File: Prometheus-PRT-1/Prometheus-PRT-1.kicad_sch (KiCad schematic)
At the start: 16 parts, among them J1 Conn_02x10_Odd_Even, J2 AppleIIBus, U1 74LS74, U2 74LS74, U3 74LS00, U4 74LS374, U5 74LS30, U6 74LS08, U7 27C64, U8 74LS08, U9 74LS00

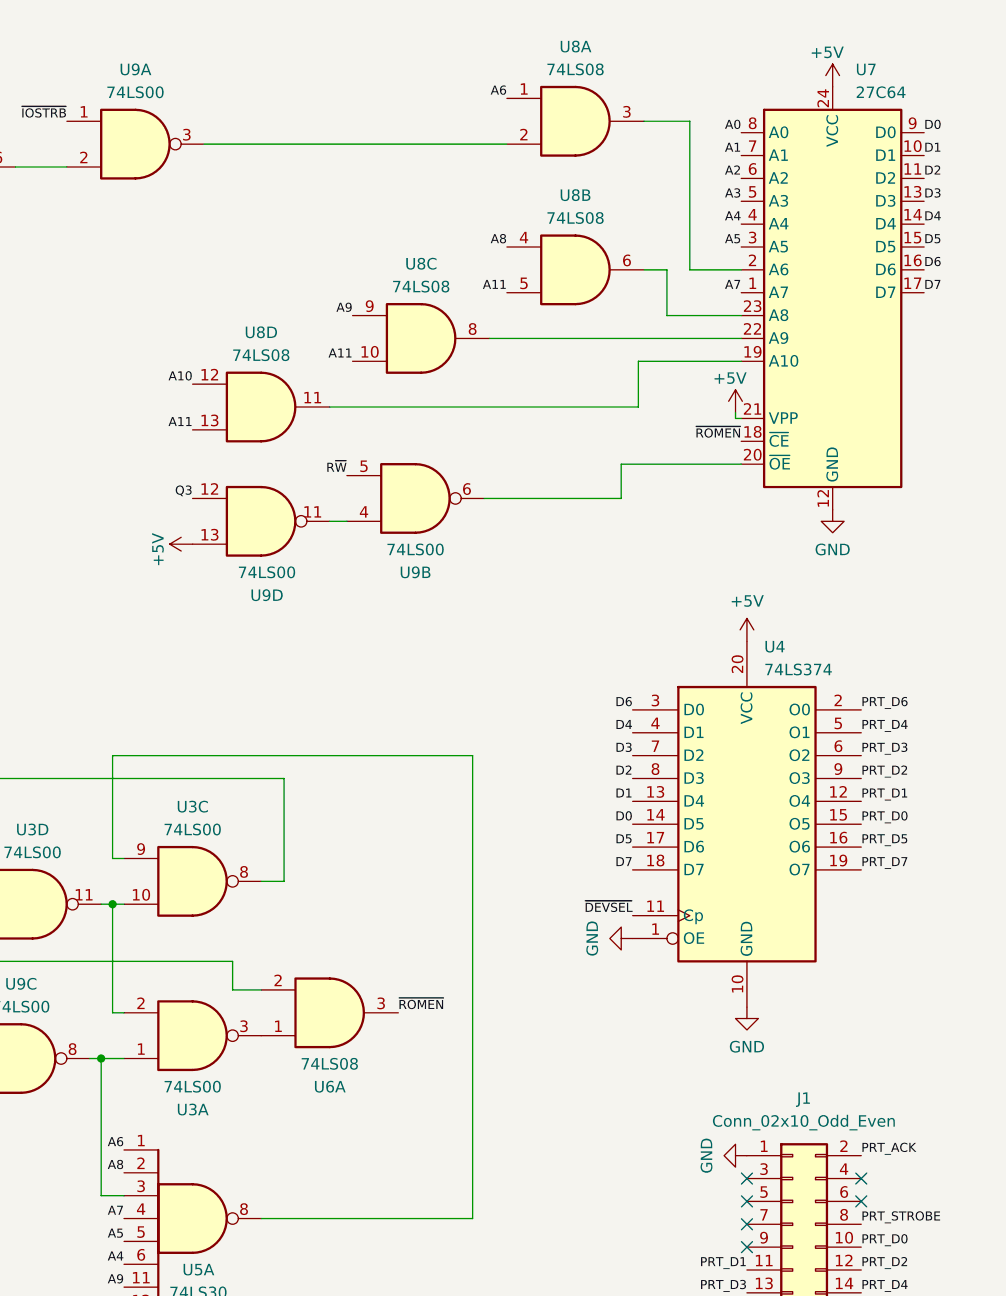
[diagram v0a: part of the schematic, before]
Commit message: Fix mis-id'd EPROM part in the PRT-1 schematic
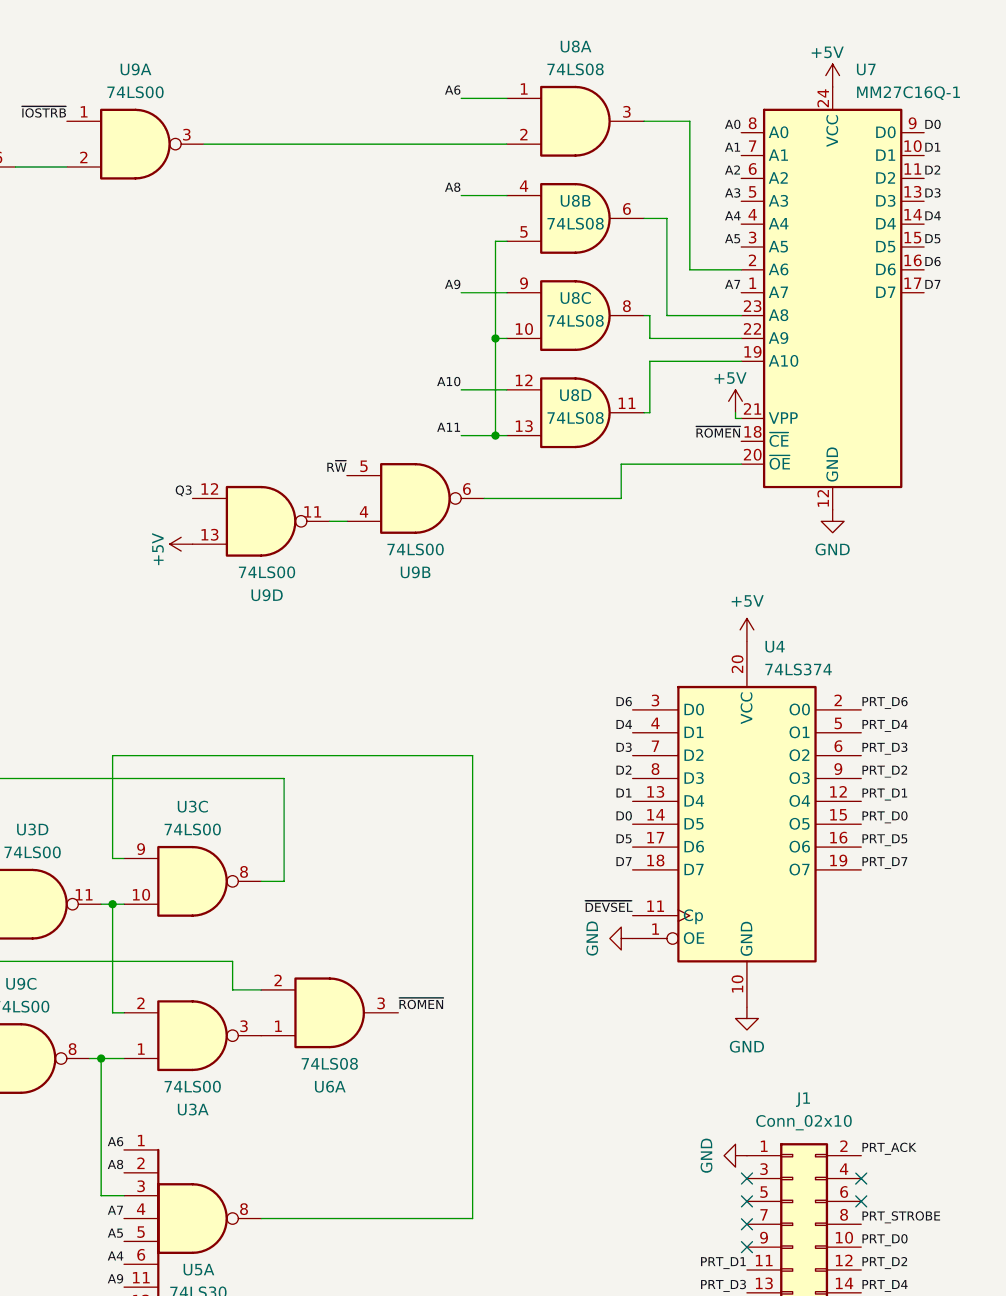
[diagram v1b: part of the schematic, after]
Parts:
- J1: value Conn_02x10_Odd_Even -> Conn_02x10
- U7: value 27C64 -> MM27C16Q-1
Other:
- moved on the sheet: U8B, U8C, U8D
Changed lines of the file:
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@@
   (junction (at 99.695 41.275) (diameter 0) (color 0 0 0 0)
   )
+  (junction (at 205.105 52.705) (diameter 0) (color 0 0 0 0)
+  )
   (junction (at 63.5 168.91) (diameter 0) (color 0 0 0 0)
   )
@@
   )
   (junction (at 49.53 168.91) (diameter 0) (color 0 0 0 0)
+  )
+  (junction (at 205.105 63.5) (diameter 0) (color 0 0 0 0)
   )
   (junction (at 109.22 102.235) (diameter 0) (color 0 0 0 0)
@@
     (stroke (width 0) (type default))
   )
-  (wire (pts (xy 220.98 55.245) (xy 232.41 55.245))
+  (wire (pts (xy 222.25 55.245) (xy 232.41 55.245))
     (stroke (width 0) (type default))
   )
@@
     (stroke (width 0) (type default))
   )
+  (wire (pts (xy 222.25 52.705) (xy 232.41 52.705))
+    (stroke (width 0) (type default))
+  )
   (wire (pts (xy 49.53 168.91) (xy 49.53 171.45))
     (stroke (width 0) (type default))
@@
     (stroke (width 0) (type default))
   )
+  (wire (pts (xy 201.295 63.5) (xy 205.105 63.5))
+    (stroke (width 0) (type default))
+  )
   (wire (pts (xy 97.155 41.91) (xy 97.155 41.275))
     (stroke (width 0) (type default))
   )
-  (wire (pts (xy 186.69 60.325) (xy 220.98 60.325))
-    (stroke (width 0) (type default))
-  )
   (wire (pts (xy 72.39 29.845) (xy 72.39 47.625))
     (stroke (width 0) (type default))
   )
+  (wire (pts (xy 205.105 52.705) (xy 205.105 63.5))
+    (stroke (width 0) (type default))
+  )
   (wire (pts (xy 114.3 86.36) (xy 114.3 104.775))
     (stroke (width 0) (type default))
@@
     (stroke (width 0) (type default))
   )
+  (wire (pts (xy 201.295 26.035) (xy 206.375 26.035))
+    (stroke (width 0) (type default))
+  )
   (wire (pts (xy 77.47 168.91) (xy 84.455 168.91))
     (stroke (width 0) (type default))
@@
     (stroke (width 0) (type default))
   )
-  (wire (pts (xy 224.155 50.165) (xy 224.155 45.085))
+  (wire (pts (xy 224.155 50.165) (xy 224.155 39.37))
     (stroke (width 0) (type default))
   )
@@
     (stroke (width 0) (type default))
   )
+  (wire (pts (xy 222.25 60.96) (xy 221.615 60.96))
+    (stroke (width 0) (type default))
+  )
+  (wire (pts (xy 206.375 52.705) (xy 205.105 52.705))
+    (stroke (width 0) (type default))
+  )
   (wire (pts (xy 63.5 191.77) (xy 63.5 194.31))
     (stroke (width 0) (type default))
@@
     (stroke (width 0) (type default))
   )
+  (wire (pts (xy 205.105 41.91) (xy 206.375 41.91))
+    (stroke (width 0) (type default))
+  )
   (wire (pts (xy 97.155 38.735) (xy 112.395 38.735))
     (stroke (width 0) (type default))
@@
     (stroke (width 0) (type default))
   )
-  (wire (pts (xy 224.155 45.085) (xy 221.615 45.085))
+  (wire (pts (xy 222.25 50.165) (xy 222.25 52.705))
+    (stroke (width 0) (type default))
+  )
+  (wire (pts (xy 224.155 39.37) (xy 221.615 39.37))
     (stroke (width 0) (type default))
   )
@@
     (stroke (width 0) (type default))
   )
+  (wire (pts (xy 201.295 36.83) (xy 206.375 36.83))
+    (stroke (width 0) (type default))
+  )
   (wire (pts (xy 105.41 168.91) (xy 119.38 168.91))
     (stroke (width 0) (type default))
@@
     (stroke (width 0) (type default))
   )
+  (wire (pts (xy 205.105 52.705) (xy 205.105 41.91))
+    (stroke (width 0) (type default))
+  )
   (wire (pts (xy 100.33 91.44) (xy 100.33 95.885))
     (stroke (width 0) (type default))
@@
     (stroke (width 0) (type default))
   )
+  (wire (pts (xy 205.105 63.5) (xy 206.375 63.5))
+    (stroke (width 0) (type default))
+  )
   (wire (pts (xy 63.5 168.91) (xy 49.53 168.91))
     (stroke (width 0) (type default))
@@
     (stroke (width 0) (type default))
   )
-  (wire (pts (xy 204.47 52.705) (xy 232.41 52.705))
+  (wire (pts (xy 221.615 50.165) (xy 222.25 50.165))
     (stroke (width 0) (type default))
   )
@@
     (stroke (width 0) (type default))
   )
-  (wire (pts (xy 220.98 60.325) (xy 220.98 55.245))
+  (wire (pts (xy 222.25 60.96) (xy 222.25 55.245))
+    (stroke (width 0) (type default))
+  )
+  (wire (pts (xy 201.295 58.42) (xy 206.375 58.42))
     (stroke (width 0) (type default))
   )
@@
   )
   (wire (pts (xy 94.615 41.91) (xy 94.615 41.275))
+    (stroke (width 0) (type default))
+  )
+  (wire (pts (xy 201.295 47.625) (xy 206.375 47.625))
     (stroke (width 0) (type default))
   )
@@
     (effects (font (size 1 1)) (justify left bottom))
   )
-  (label "A11" (at 189.23 55.245 180) (fields_autoplaced)
-    (effects (font (size 1 1)) (justify right bottom))
-  )
   (label "PRT_D0" (at 245.745 106.68 0) (fields_autoplaced)
     (effects (font (size 1 1)) (justify left bottom))
@@
     (effects (font (size 1 1)) (justify left bottom))
   )
-  (label "A6" (at 206.375 26.035 180) (fields_autoplaced)
+  (label "A6" (at 201.295 26.035 180) (fields_autoplaced)
     (effects (font (size 1 1)) (justify right bottom))
   )
@@
     (effects (font (size 1 1)) (justify left bottom))
   )
-  (label "A9" (at 189.23 50.165 180) (fields_autoplaced)
+  (label "A9" (at 201.295 47.625 180) (fields_autoplaced)
     (effects (font (size 1 1)) (justify right bottom))
   )
@@
     (effects (font (size 1 1)) (justify right bottom))
   )
-  (label "A11" (at 171.45 62.865 180) (fields_autoplaced)
+  (label "A11" (at 201.295 63.5 180) (fields_autoplaced)
     (effects (font (size 1 1)) (justify right bottom))
   )
@@
     (effects (font (size 1 1)) (justify right bottom))
   )
-  (label "A11" (at 206.375 47.625 180) (fields_autoplaced)
-    (effects (font (size 1 1)) (justify right bottom))
-  )
-  (label "A8" (at 206.375 42.545 180) (fields_autoplaced)
+  (label "A8" (at 201.295 36.83 180) (fields_autoplaced)
     (effects (font (size 1 1)) (justify right bottom))
   )
@@
     (effects (font (size 1 1)) (justify right bottom))
   )
-  (label "A10" (at 171.45 57.785 180) (fields_autoplaced)
+  (label "A10" (at 201.295 58.42 180) (fields_autoplaced)
     (effects (font (size 1 1)) (justify right bottom))
   )
@@
       (effects (font (size 1.27 1.27)))
     )
-    (property "Value" "Conn_02x10_Odd_Even" (at 239.395 139.7 0)
+    (property "Value" "Conn_02x10" (at 239.395 139.7 0)
       (effects (font (size 1.27 1.27)))
     )
@@
       (effects (font (size 1.27 1.27)) (justify left))
     )
-    (property "Value" "27C64" (at 245.11 25.4 0)
+    (property "Value" "MM27C16Q-1" (at 245.11 25.4 0)
       (effects (font (size 1.27 1.27)) (justify left))
     )
@@
     )
   )
-  (symbol (lib_id "74xx:74LS08") (at 196.85 52.705 0) (unit 3)
-    (in_bom yes) (on_board yes) (dnp no)
-    (property "Reference" "U8" (at 196.8417 44.45 0)
-      (effects (font (size 1.27 1.27)))
-    )
-    (property "Value" "74LS08" (at 196.8417 46.99 0)
-      (effects (font (size 1.27 1.27)))
-    )
-    (property "Footprint" "Package_DIP:DIP-14_W7.62mm_Socket_LongPads" (at 196.85 52.705 0)
-      (effects (font (size 1.27 1.27)) hide)
-    )
-    (property "Datasheet" "http://www.ti.com/lit/gpn/sn74LS08" (at 196.85 52.705 0)
+  (symbol (lib_id "74xx:74LS08") (at 213.995 50.165 0) (unit 3)
+    (in_bom yes) (on_board yes) (dnp no)
+    (property "Reference" "U8" (at 213.995 48.26 0)
+      (effects (font (size 1.27 1.27)))
+    )
+    (property "Value" "74LS08" (at 213.995 50.8 0)
+      (effects (font (size 1.27 1.27)))
+    )
+    (property "Footprint" "Package_DIP:DIP-14_W7.62mm_Socket_LongPads" (at 213.995 50.165 0)
+      (effects (font (size 1.27 1.27)) hide)
+    )
+    (property "Datasheet" "http://www.ti.com/lit/gpn/sn74LS08" (at 213.995 50.165 0)
       (effects (font (size 1.27 1.27)) hide)
     )
@@
     )
   )
-  (symbol (lib_id "74xx:74LS08") (at 179.07 60.325 0) (unit 4)
-    (in_bom yes) (on_board yes) (dnp no)
-    (property "Reference" "U8" (at 179.07 52.07 0)
-      (effects (font (size 1.27 1.27)))
-    )
-    (property "Value" "74LS08" (at 179.07 54.61 0)
-      (effects (font (size 1.27 1.27)))
-    )
-    (property "Footprint" "Package_DIP:DIP-14_W7.62mm_Socket_LongPads" (at 179.07 60.325 0)
-      (effects (font (size 1.27 1.27)) hide)
-    )
-    (property "Datasheet" "http://www.ti.com/lit/gpn/sn74LS08" (at 179.07 60.325 0)
+  (symbol (lib_id "74xx:74LS08") (at 213.995 60.96 0) (unit 4)
+    (in_bom yes) (on_board yes) (dnp no)
+    (property "Reference" "U8" (at 213.995 59.055 0)
+      (effects (font (size 1.27 1.27)))
+    )
+    (property "Value" "74LS08" (at 213.995 61.595 0)
+      (effects (font (size 1.27 1.27)))
+    )
+    (property "Footprint" "Package_DIP:DIP-14_W7.62mm_Socket_LongPads" (at 213.995 60.96 0)
+      (effects (font (size 1.27 1.27)) hide)
+    )
+    (property "Datasheet" "http://www.ti.com/lit/gpn/sn74LS08" (at 213.995 60.96 0)
       (effects (font (size 1.27 1.27)) hide)
     )
@@
     )
   )
-  (symbol (lib_id "74xx:74LS08") (at 213.995 45.085 0) (unit 2)
-    (in_bom yes) (on_board yes) (dnp no)
-    (property "Reference" "U8" (at 213.9867 36.83 0)
-      (effects (font (size 1.27 1.27)))
-    )
-    (property "Value" "74LS08" (at 213.9867 39.37 0)
-      (effects (font (size 1.27 1.27)))
-    )
-    (property "Footprint" "Package_DIP:DIP-14_W7.62mm_Socket_LongPads" (at 213.995 45.085 0)
-      (effects (font (size 1.27 1.27)) hide)
-    )
-    (property "Datasheet" "http://www.ti.com/lit/gpn/sn74LS08" (at 213.995 45.085 0)
-      (effects (font (size 1.27 1.27)) hide)
-    )
+  (symbol (lib_id "74xx:74LS08") (at 213.995 39.37 0) (unit 2)
+    (in_bom yes) (on_board yes) (dnp no)
+    (property "Reference" "U8" (at 213.995 37.465 0)
+      (effects (font (size 1.27 1.27)))
+    )
+    (property "Value" "74LS08" (at 213.995 40.005 0)
+      (effects (font (size 1.27 1.27)))
+    )
+    (property "Footprint" "Package_DIP:DIP-14_W7.62mm_Socket_LongPads" (at 213.995 39.37 0)
+      (effects (font (size 1.27 1.27)) hide)
+    )
+    (property "Datasheet" "http://www.ti.com/lit/gpn/sn74LS08" (at 213.995 39.37 0)
+      (effects (font (size 1.27 1.27)) hide)
+    )
